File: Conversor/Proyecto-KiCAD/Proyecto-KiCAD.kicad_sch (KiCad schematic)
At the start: 44 parts, among them Q1 IRFP150, Q2 IRFP150, Q3 IRFP150, Q4 IRFP150

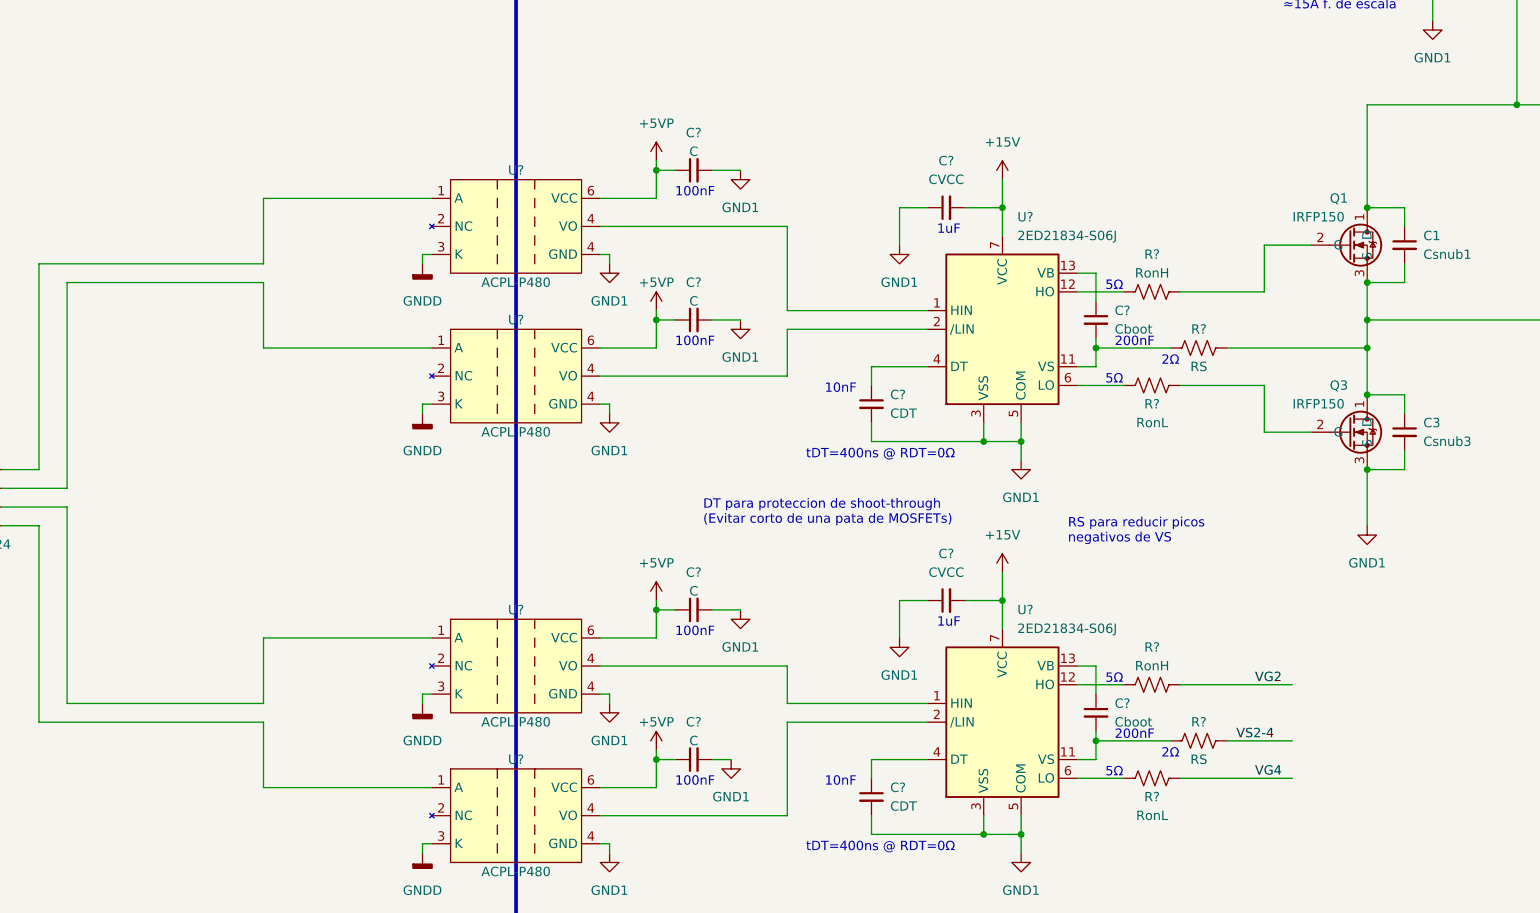
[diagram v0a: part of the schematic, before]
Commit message: Agregar alimentacion de 10V para los drivers
- Usar LM2576T-ADJ para obtener salida de 10V con 3A de Iout_max (1.1A
por driver se necesitan)
  - Preguntar si esta bien, porque requiere un inductor de 100uH, si no
usar alimentacion externa de 24V y un regulador normal de 15V
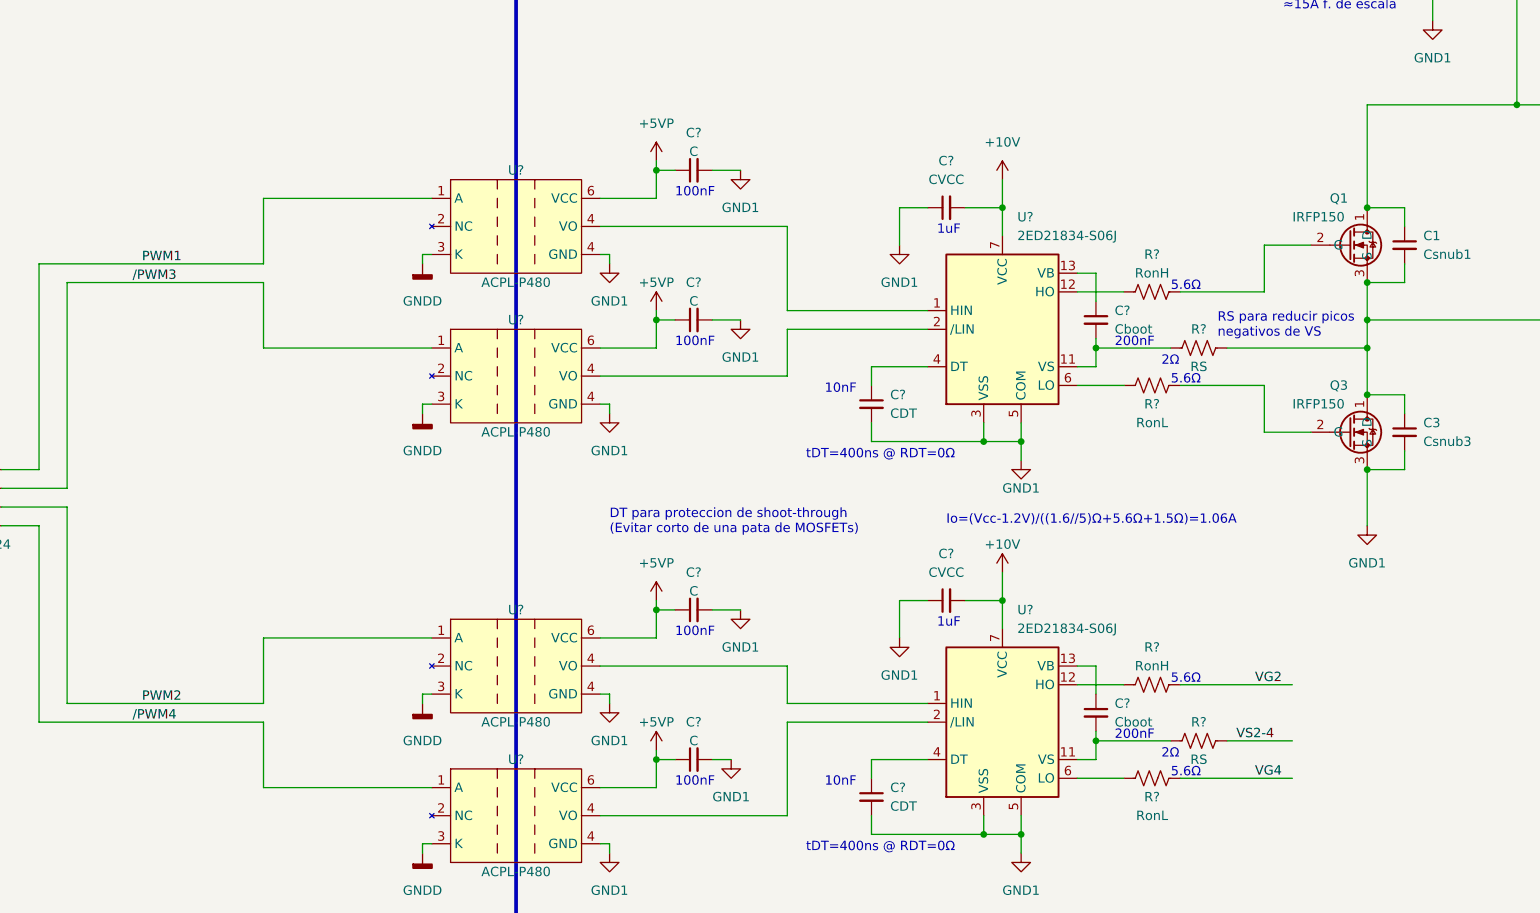
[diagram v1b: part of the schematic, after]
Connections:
- net PWM2: now reaches J?.3 (Pin_3), U?.1 (A)
- net PWM1: now reaches J?.1 (Pin_1), U?.1 (A)
- net /PWM3: now reaches J?.2 (Pin_2), U?.1 (A)
- net /PWM4: now reaches J?.4 (Pin_4), U?.1 (A)
- net +15V renamed +10V
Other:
- note added: "5.6Ω"
- note added: "Io=(Vcc-1.2V)/((1.6//5)Ω+5.6Ω+1.5Ω)=1.06A"
- note removed: "5Ω"

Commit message: Empezar a arreglar los errores del ERC de KiCad
- Quedan muchos warnings pero un error de input power pin not driven
- Hay que hacer el esquematico general con alimentacion y preguntar
sobre el regulador de 10V
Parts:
- removed U?: 2ED21834-S06J, Package_SO:SOIC-14_3.9x8.7mm_P1.27mm, symbol Componentes proyecto:2ED21834-S06J
- added U5: 2ED21834-S06J, symbol Componentes proyecto:2ED21834-S06J
- gave numbers to parts that had none: 31
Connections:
- net +10V: now also U5.7 (VCC)
- net GND1: now also U5.3 (VSS), U5.5 (COM)
- net at C13.1: now also U5.13 (VB)
- net at C13.2, R5.1: now also U5.11 (VS)
- net at R1.1: now also U5.12 (HO)
- net at C9.1: now also U5.4 (DT)
- net at R2.1: now also U5.6 (LO)
- net IOUT- renamed IOUT-/VOUT
- new net: U1.4 (VO), U5.1 (HIN)
- new net: U2.4 (VO), U5.2 (/LIN)

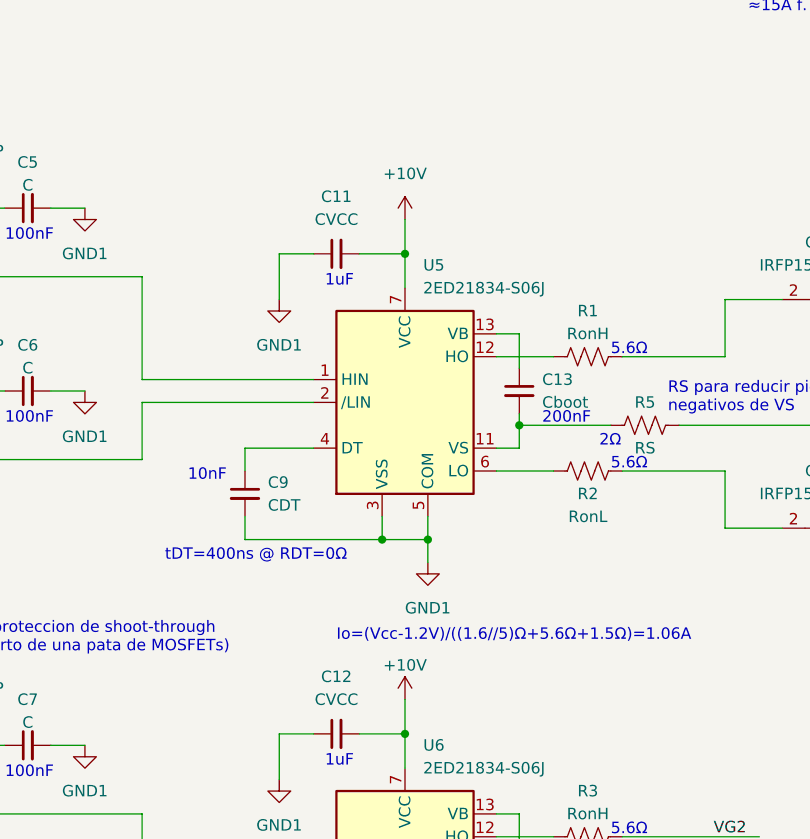
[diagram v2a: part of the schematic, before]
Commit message: Comenzar el diagrama mas detallado (en draw.io)
- Remover el regulador de 10V para los drivers, ahora se alimentan
directamente desde los 12-18V sin regulación
- Por hacer:
  - Falta agregar la alimentación y algunos labels en el    diagrama
  - Remover la hoja de datos del regulador de 10V
  - Pasar todos los componentes a subsheets como en la placa adaptadora,
de manera que quede como un diagrama de bloques
  - Una vez hecho eso, agregar el circuito de la placa adaptadora al
proyecto (tiene que ser todo una plaqueta)
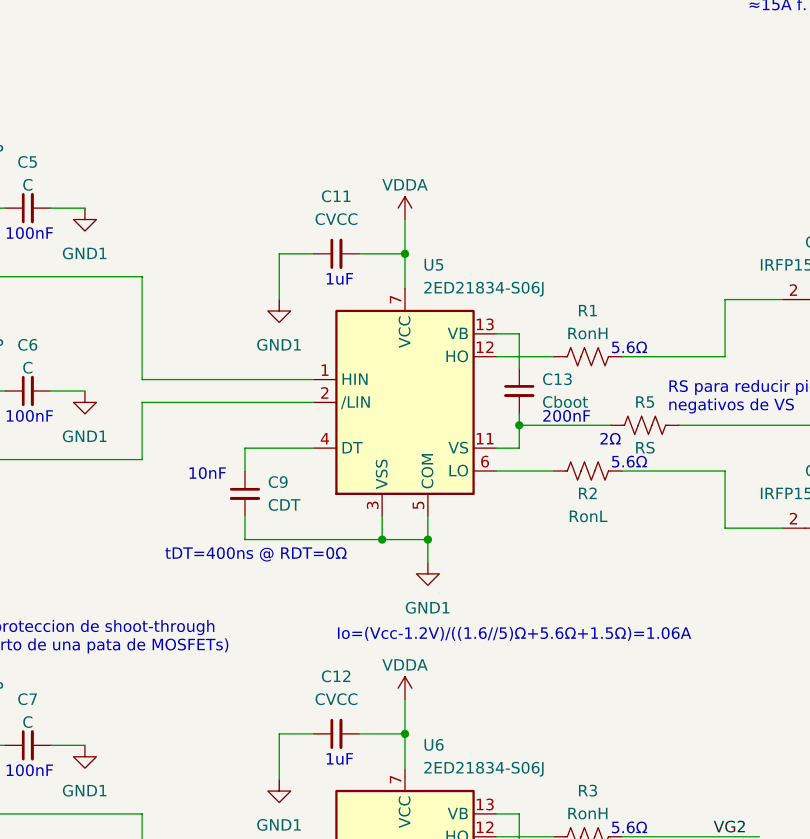
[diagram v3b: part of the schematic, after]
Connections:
- net +10V renamed VDDA
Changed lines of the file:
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@@
     (pin "2")
-  )
-  (symbol (lib_id "power:+10V") (at 162.56 133.35 0) (unit 1)
-    (in_bom yes) (on_board yes) (fields_autoplaced)
-    (property "Reference" "#PWR0112" (id 0) (at 162.56 137.16 0)
-      (effects (font (size 1.27 1.27)) hide)
-    )
-    (property "Value" "+10V" (id 1) (at 162.56 128.27 0))
-    (property "Footprint" "" (id 2) (at 162.56 133.35 0)
-      (effects (font (size 1.27 1.27)) hide)
-    )
-    (property "Datasheet" "" (id 3) (at 162.56 133.35 0)
-      (effects (font (size 1.27 1.27)) hide)
-    )
-    (pin "1")
   )
   (symbol (lib_id "power:GND1") (at 109.22 224.79 0) (unit 1)
@@
     (pin "1")
   )
+  (symbol (lib_id "power:VDDA") (at 162.56 186.69 0) (unit 1)
+    (in_bom yes) (on_board yes)
+    (property "Reference" "#PWR0104" (id 0) (at 162.56 190.5 0)
+      (effects (font (size 1.27 1.27)) hide)
+    )
+    (property "Value" "VDDA" (id 1) (at 162.56 182.88 0))
+    (property "Footprint" "" (id 2) (at 162.56 186.69 0)
+      (effects (font (size 1.27 1.27)) hide)
+    )
+    (property "Datasheet" "" (id 3) (at 162.56 186.69 0)
+      (effects (font (size 1.27 1.27)) hide)
+    )
+    (pin "1")
+  )
   (symbol (lib_id "power:PWR_FLAG") (at 318.77 168.91 270) (unit 1)
     (in_bom yes) (on_board yes) (fields_autoplaced)
@@
     (pin "2")
   )
+  (symbol (lib_id "power:VDDA") (at 162.56 133.35 0) (unit 1)
+    (in_bom yes) (on_board yes)
+    (property "Reference" "#PWR0112" (id 0) (at 162.56 137.16 0)
+      (effects (font (size 1.27 1.27)) hide)
+    )
+    (property "Value" "VDDA" (id 1) (at 162.56 129.54 0))
+    (property "Footprint" "" (id 2) (at 162.56 133.35 0)
+      (effects (font (size 1.27 1.27)) hide)
+    )
+    (property "Datasheet" "" (id 3) (at 162.56 133.35 0)
+      (effects (font (size 1.27 1.27)) hide)
+    )
+    (pin "1")
+  )
   (symbol (lib_id "power:+5VP") (at 115.57 210.82 0) (unit 1)
     (in_bom yes) (on_board yes)
@@
     (pin "1")
     (pin "2")
-  )
-  (symbol (lib_id "power:+10V") (at 162.56 186.69 0) (unit 1)
-    (in_bom yes) (on_board yes)
-    (property "Reference" "#PWR0104" (id 0) (at 162.56 190.5 0)
-      (effects (font (size 1.27 1.27)) hide)
-    )
-    (property "Value" "+10V" (id 1) (at 162.56 182.88 0))
-    (property "Footprint" "" (id 2) (at 162.56 186.69 0)
-      (effects (font (size 1.27 1.27)) hide)
-    )
-    (property "Datasheet" "" (id 3) (at 162.56 186.69 0)
-      (effects (font (size 1.27 1.27)) hide)
-    )
-    (pin "1")
   )
   (symbol (lib_name "ACPL-P480_2") (lib_id "Componentes proyecto:ACPL-P480") (at 96.52 199.39 0) (unit 1)
@@
       (reference "#FLG0103") (unit 1) (value "PWR_FLAG") (footprint "")
     )
-    (path "/59d8992c-71f3-4d96-a665-43f8d7d91dab/c551a176-3eca-47e1-88b7-11fb1f4eec67"
-      (reference "#FLG0104") (unit 1) (value "PWR_FLAG") (footprint "")
-    )
     (path "/02b36b52-6a67-4b1a-aeda-ca74c124cf8d/f73698a8-3de1-4678-a688-c220e770e30e"
       (reference "#FLG0105") (unit 1) (value "PWR_FLAG") (footprint "")
@@
       (reference "#PWR0103") (unit 1) (value "GND1") (footprint "")
     )
-    (path "/b74893ef-c260-40e7-8209-5d840ce53541"
-      (reference "#PWR0104") (unit 1) (value "+10V") (footprint "")
+    (path "/75552e51-aac3-4cd1-b8f4-3daa70ece248"
+      (reference "#PWR0104") (unit 1) (value "VDDA") (footprint "")
     )
     (path "/0b7b06c2-eddc-4c0e-9041-c04f576218bc"
@@
       (reference "#PWR0111") (unit 1) (value "GND1") (footprint "")
     )
-    (path "/07b2da65-1825-486e-ae29-0ef2d0371d00"
-      (reference "#PWR0112") (unit 1) (value "+10V") (footprint "")
+    (path "/a2916a14-5fd3-4ec2-893b-1c0391c71289"
+      (reference "#PWR0112") (unit 1) (value "VDDA") (footprint "")
     )
     (path "/95eb5cdd-7714-4dcb-af23-b9b1b8518d4a"
@@
       (reference "#PWR0158") (unit 1) (value "GND1") (footprint "")
     )
-    (path "/59d8992c-71f3-4d96-a665-43f8d7d91dab/3d1a03e6-4a51-4cd8-beb7-f4c4e1032574"
-      (reference "#PWR0159") (unit 1) (value "GND1") (footprint "")
-    )
     (path "/40ada2ea-a259-4aaf-a47d-4f1bafebc3ab"
       (reference "C1") (unit 1) (value "Csnub1") (footprint "")
@@
       (reference "C27") (unit 1) (value "C") (footprint "")
     )
-    (path "/59d8992c-71f3-4d96-a665-43f8d7d91dab/c96b5793-aefc-4c7f-9fcb-3342464bea01"
-      (reference "C28") (unit 1) (value "CREGin") (footprint "")
-    )
     (path "/59d8992c-71f3-4d96-a665-43f8d7d91dab/c06d6c45-819d-45e2-90be-511deb13cd0e"
       (reference "C29") (unit 1) (value "CREG_IN") (footprint "")
@@
       (reference "D5") (unit 1) (value "MBR0520") (footprint "Diode_SMD:D_SOD-123")
     )
-    (path "/59d8992c-71f3-4d96-a665-43f8d7d91dab/fb68a379-dd80-4a1c-aa86-99bb5d3288c5"
-      (reference "D6") (unit 1) (value "MBR340") (footprint "Diode_THT:D_DO-201AD_P15.24mm_Horizontal")
-    )
     (path "/bcaf2dca-bfb6-45b7-bff9-b0d7d064715a"
       (reference "J1") (unit 1) (value "ConnPWM1324") (footprint "")
@@
       (reference "J7") (unit 1) (value "ConnAlim12-18") (footprint "")
     )
-    (path "/59d8992c-71f3-4d96-a665-43f8d7d91dab/455b6c81-fc7d-403c-a3f8-0e5597541c5d"
-      (reference "L1") (unit 1) (value "L") (footprint "")
-    )
     (path "/7c4723ef-9098-48c6-a170-8710177e4d8e"
       (reference "Q1") (unit 1) (value "IRFP150") (footprint "Package_TO_SOT_THT:TO-247-3_Vertical")
@@
       (reference "R20") (unit 1) (value "R") (footprint "")
     )
-    (path "/59d8992c-71f3-4d96-a665-43f8d7d91dab/07b09dec-6b3b-48a6-bfc6-7b2476162937"
-      (reference "R21") (unit 1) (value "R2") (footprint "")
-    )
-    (path "/59d8992c-71f3-4d96-a665-43f8d7d91dab/5d4b47d3-2d08-4bc3-93db-ce441235acad"
-      (reference "R22") (unit 1) (value "R1") (footprint "")
-    )
     (path "/f6b3adcb-0799-42a8-87ad-7d3738e77a1e"
       (reference "U1") (unit 1) (value "ACPL-P480") (footprint "Package_SO:SSO-6_6.8x4.6mm_P1.27mm_Clearance7mm")
@@
       (reference "U11") (unit 1) (value "LM7805_TO220") (footprint "Package_TO_SOT_THT:TO-220-3_Vertical")
     )
-    (path "/59d8992c-71f3-4d96-a665-43f8d7d91dab/8e6752df-f11d-43f7-ab81-61ef784878ab"
-      (reference "U12") (unit 1) (value "LM2576HVS-ADJ") (footprint "Package_TO_SOT_SMD:TO-263-5_TabPin3")
-    )
     (path "/59d8992c-71f3-4d96-a665-43f8d7d91dab/581089b1-75b4-48f9-abac-91a1bf7fabba"

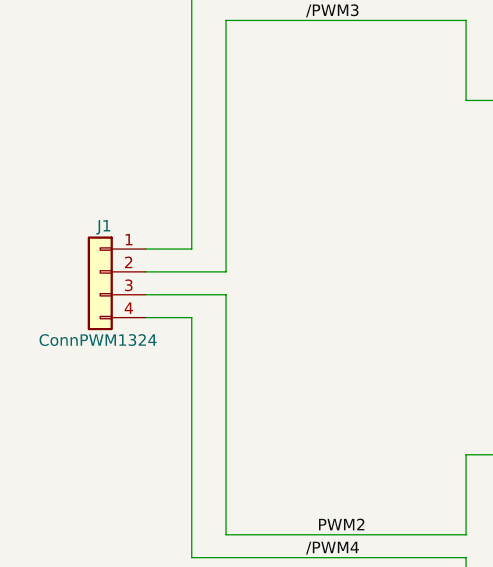
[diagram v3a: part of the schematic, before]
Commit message: Finalizar el diagrama detallado
Por hacer:
  - Reoriganizar el esquemático de KiCad como pidió Jorge
  - Preguntar sobre la alimentación de la placa adaptadora
  - Incorporar la placa adaptadora al diseño
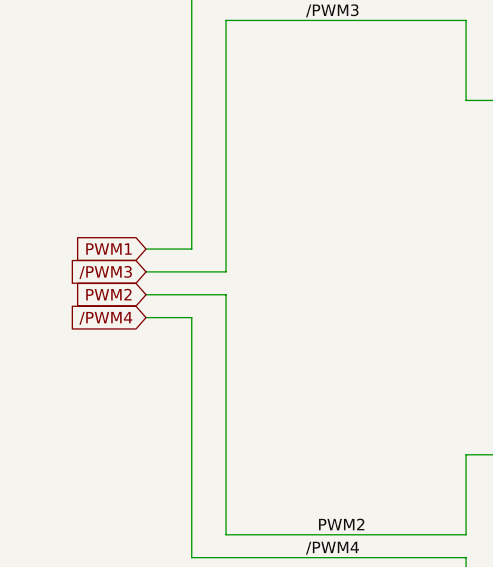
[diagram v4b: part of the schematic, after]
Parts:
- removed J1: ConnPWM1324, symbol Connector_Generic:Conn_01x04
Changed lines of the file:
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@@
+    )
+  )
+  (global_label "{slash}PWM3" (shape input) (at 26.67 175.26 180) (fields_autoplaced)
+    (effects (font (size 1.27 1.27)) (justify right))
+    (property "Intersheet References" "${INTERSHEET_REFS}" (id 0) (at 17.544 175.1806 0)
+      (effects (font (size 1.27 1.27)) (justify right) hide)
     )
   )
@@
     )
   )
+  (global_label "PWM2" (shape input) (at 26.67 177.8 180) (fields_autoplaced)
+    (effects (font (size 1.27 1.27)) (justify right))
+    (property "Intersheet References" "${INTERSHEET_REFS}" (id 0) (at 18.8745 177.7206 0)
+      (effects (font (size 1.27 1.27)) (justify right) hide)
+    )
+  )
+  (global_label "PWM1" (shape input) (at 26.67 172.72 180) (fields_autoplaced)
+    (effects (font (size 1.27 1.27)) (justify right))
+    (property "Intersheet References" "${INTERSHEET_REFS}" (id 0) (at 18.8745 172.6406 0)
+      (effects (font (size 1.27 1.27)) (justify right) hide)
+    )
+  )
+  (global_label "{slash}PWM4" (shape input) (at 26.67 180.34 180) (fields_autoplaced)
+    (effects (font (size 1.27 1.27)) (justify right))
+    (property "Intersheet References" "${INTERSHEET_REFS}" (id 0) (at 17.544 180.2606 0)
+      (effects (font (size 1.27 1.27)) (justify right) hide)
+    )
+  )
   (global_label "IFC+" (shape passive) (at 207.01 76.2 90) (fields_autoplaced)
     (effects (font (size 1.27 1.27)) (justify left))
@@
     (pin "4")
     (pin "6")
-  )
-  (symbol (lib_id "Connector_Generic:Conn_01x04") (at 21.59 175.26 0) (mirror y) (unit 1)
-    (in_bom yes) (on_board yes)
-    (property "Reference" "J1" (id 0) (at 22.86 170.18 0)
-      (effects (font (size 1.27 1.27)) (justify left))
-    )
-    (property "Value" "ConnPWM1324" (id 1) (at 27.94 182.88 0)
-      (effects (font (size 1.27 1.27)) (justify left))
-    )
-    (property "Footprint" "" (id 2) (at 21.59 175.26 0)
-      (effects (font (size 1.27 1.27)) hide)
-    )
-    (property "Datasheet" "~" (id 3) (at 21.59 175.26 0)
-      (effects (font (size 1.27 1.27)) hide)
-    )
-    (pin "1")
-    (pin "2")
-    (pin "3")
-    (pin "4")
   )
   (symbol (lib_id "Componentes proyecto:MUR860") (at 337.82 146.05 0) (unit 1)
@@
       (reference "D5") (unit 1) (value "MBR0520") (footprint "Diode_SMD:D_SOD-123")
     )
-    (path "/bcaf2dca-bfb6-45b7-bff9-b0d7d064715a"
-      (reference "J1") (unit 1) (value "ConnPWM1324") (footprint "")
-    )
     (path "/82aabcfc-0d2e-42ec-8d77-046e7fec23ed"
